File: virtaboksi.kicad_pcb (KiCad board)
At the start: 2 copper layers, 50 x 72 mm, 64 parts, among them J1 Panel_01x06, J2 External_01x06, J3 Optional_01x03, J5 Powerpole 01x02, J6 Powerpole 01x02, J7 Powerpole 01x02, J8 TagConnect_TC2030-NL, Q1 2N7002, Q2 IRF4905, Q3 IRF4905, Q4 2N7002, Q5 IRF4905, Q6 IRF4905, Q7 2N7002, Q8 IRF4905, Q9 IRF4905, U1 SRV05-4, U2 AMSRI-783.3-NZ, U3 SRV05-4, U4 SP3485EN, U5 STM8S003F3P

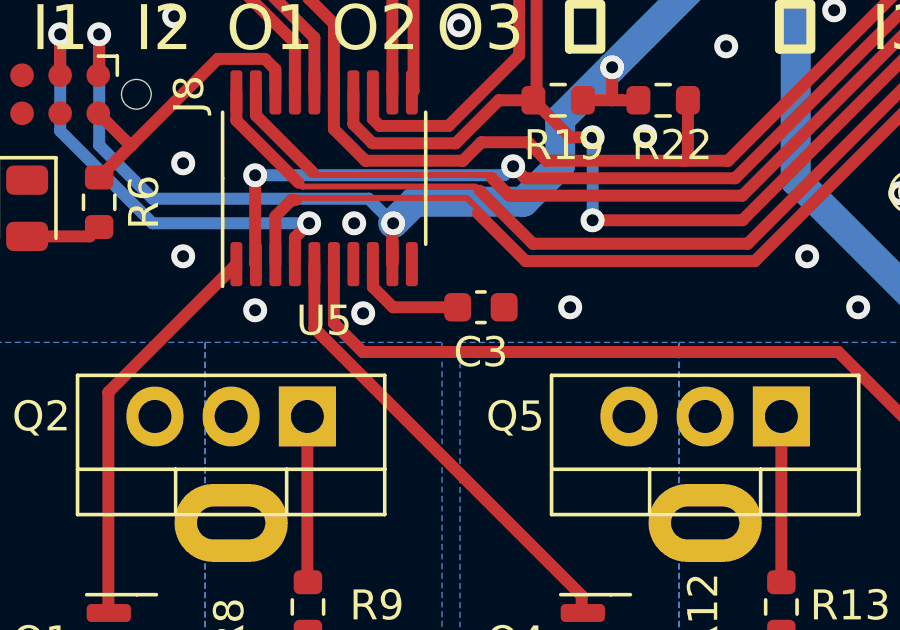
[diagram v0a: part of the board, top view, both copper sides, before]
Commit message: Move STM8S capacitor out of way
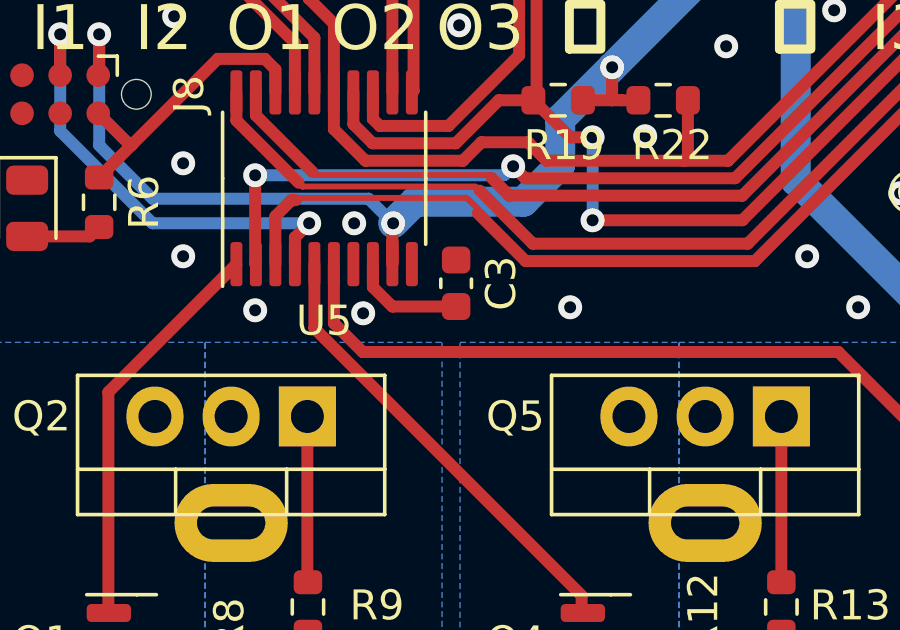
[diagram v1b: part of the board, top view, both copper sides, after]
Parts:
- moved C3 1.15 mm to (123.2, 61.9), turned to 90 degrees
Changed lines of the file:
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@@
   )
   (footprint "Capacitor_SMD:C_0603_1608Metric" (layer "F.Cu")
-    (at 124.025 62.7)
+    (at 123.2 61.9 90)
     (descr "Capacitor SMD 0603 (1608 Metric), square (rectangular) end terminal, IPC_7351 nominal, (Body size source: IPC-SM-782 page 76, https://www.pcb-3d.com/wordpress/wp-content/uploads/ipc-sm-782a_amendment_1_and_2.pdf), generated with kicad-footprint-generator")
     (tags "capacitor")
@@
     (property "Sheetname" "")
     (attr smd)
-    (fp_text reference "C3" (at 0 1.5) (layer "F.SilkS")
+    (fp_text reference "C3" (at 0 1.5 90) (layer "F.SilkS")
       (effects (font (size 1 1) (thickness 0.15)))
     )
-    (fp_text value "1u" (at 0 1.43) (layer "F.Fab")
+    (fp_text value "1u" (at 0 1.43 90) (layer "F.Fab")
       (effects (font (size 1 1) (thickness 0.15)))
     )
-    (fp_text user "${REFERENCE}" (at 0 0) (layer "F.Fab")
+    (fp_text user "${REFERENCE}" (at 0 0 90) (layer "F.Fab")
       (effects (font (size 0.4 0.4) (thickness 0.06)))
     )
@@
     (fp_line (start -0.8 0.4) (end -0.8 -0.4) (layer "F.Fab") (width 0.1))
     (fp_line (start -0.8 -0.4) (end 0.8 -0.4) (layer "F.Fab") (width 0.1))
-    (pad "1" smd roundrect (at -0.775 0) (size 0.9 0.95) (layers "F.Cu" "F.Paste" "F.Mask") (roundrect_rratio 0.25)
+    (pad "1" smd roundrect (at -0.775 0 90) (size 0.9 0.95) (layers "F.Cu" "F.Paste" "F.Mask") (roundrect_rratio 0.25)
       (net 8 "Net-(C3-Pad1)") (pintype "passive"))
-    (pad "2" smd roundrect (at 0.775 0) (size 0.9 0.95) (layers "F.Cu" "F.Paste" "F.Mask") (roundrect_rratio 0.25)
+    (pad "2" smd roundrect (at 0.775 0 90) (size 0.9 0.95) (layers "F.Cu" "F.Paste" "F.Mask") (roundrect_rratio 0.25)
       (net 1 "GND") (pintype "passive"))
     (model "${KICAD6_3DMODEL_DIR}/Capacitor_SMD.3dshapes/C_0603_1608Metric.wrl"
@@
   (segment (start 127.3825 72.85) (end 127.4225 72.89) (width 0.4) (layer "F.Cu") (net 7))
   (segment (start 118.475 61.2625) (end 118.475 63.400843) (width 0.4) (layer "F.Cu") (net 7))
-  (segment (start 121.096177 62.7) (end 123.25 62.7) (width 0.4) (layer "F.Cu") (net 8))
-  (segment (start 120.425 61.2625) (end 120.425 62.028823) (width 0.4) (layer "F.Cu") (net 8))
-  (segment (start 120.425 62.028823) (end 121.096177 62.7) (width 0.4) (layer "F.Cu") (net 8))
+  (segment (start 121.071177 62.675) (end 120.425 62.028823) (width 0.4) (layer "F.Cu") (net 8))
+  (segment (start 120.425 62.028823) (end 120.425 61.2625) (width 0.4) (layer "F.Cu") (net 8))
+  (segment (start 123.2 62.675) (end 121.071177 62.675) (width 0.4) (layer "F.Cu") (net 8))
   (segment (start 149.86 75.065) (end 151.71 76.915) (width 0.4) (layer "F.Cu") (net 9))
   (segment (start 147.14 76.615) (end 148.31 76.615) (width 0.4) (layer "F.Cu") (net 9))

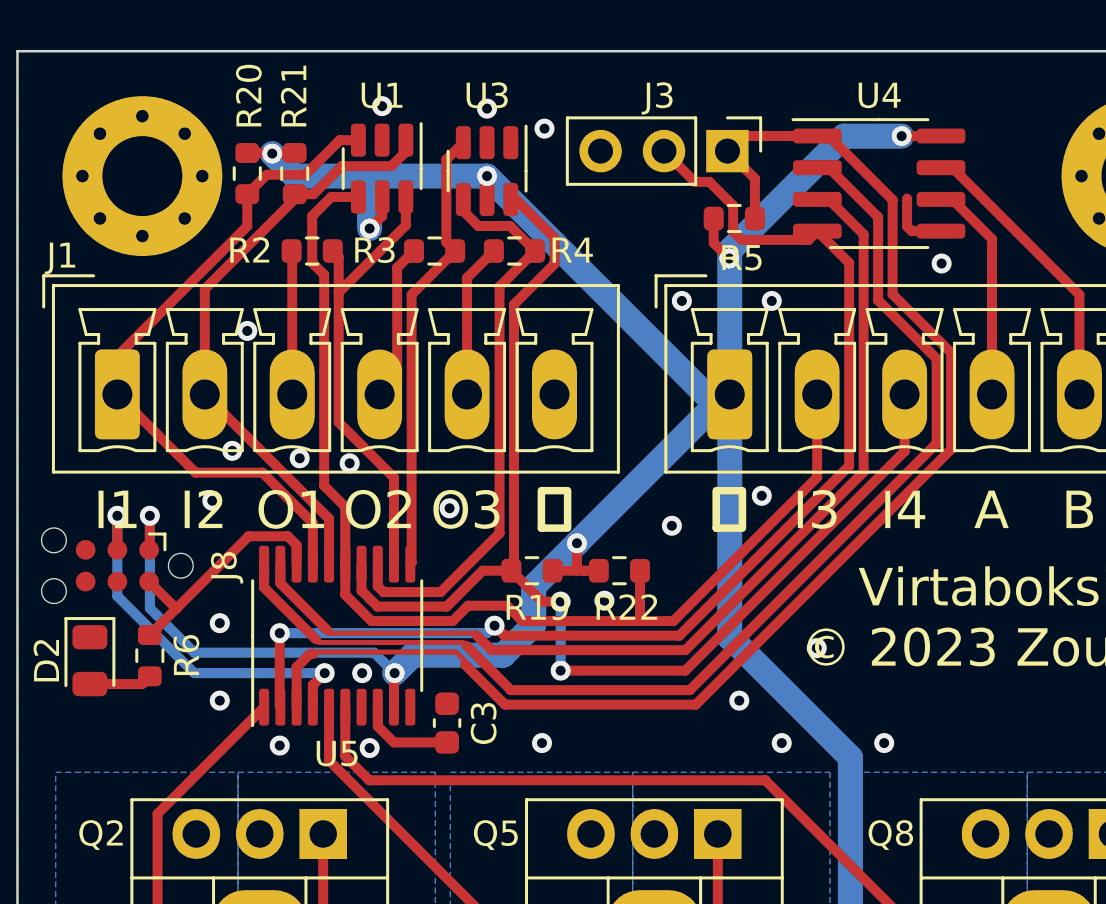
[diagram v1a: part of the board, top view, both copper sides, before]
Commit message: Final tweaks to the PCB. Swap LED pins for better routing.
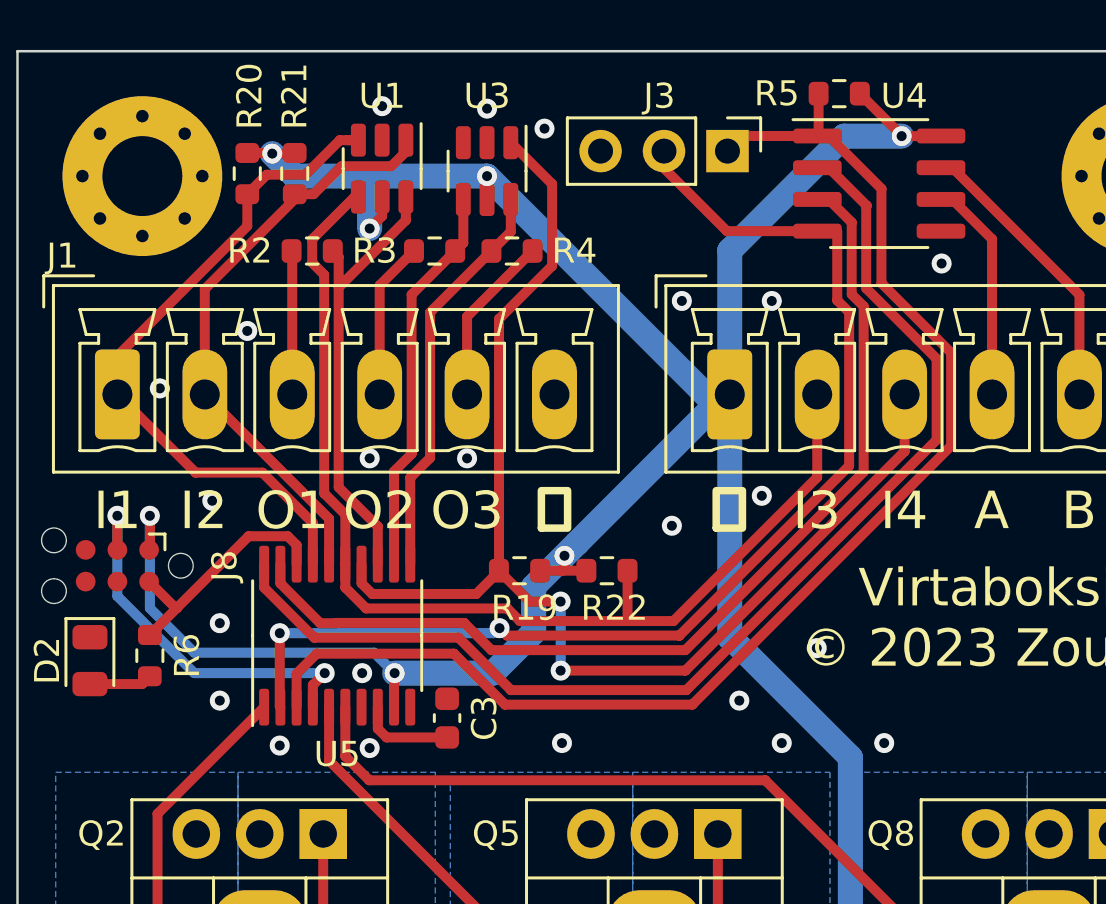
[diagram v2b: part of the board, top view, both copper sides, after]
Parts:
- moved R5 6.53 mm to (138.9, 36.7), turned to 180 degrees
- moved R19 0.50 mm to (126.1, 55.8)
- moved R22 0.50 mm to (129.6, 55.8)
- moved C3 0.20 mm to (123.2, 61.7)
- moved R4 0.10 mm to (125.8, 43.0), turned to 180 degrees
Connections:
- U3 pad 1: unconnected-(U3-Pad1) -> /IN4
- U3 pad 3: /LED2 -> unconnected-(U3-Pad3)
- U3 pad 4: /LED3 -> /LED2
- U3 pad 6: /IN4 -> /LED3
- U5 pad 11: /LED2 -> /LED3
- U5 pad 12: /LED1 -> /LED2
- U5 pad 13: /LED3 -> /LED1
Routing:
- net /LED3: track 22.7 -> 16.3 mm
- net GND: track 2.55 -> 0.00 mm, vias 29 -> 27
- net /LED2: track 18.0 -> 15.7 mm
- net /RX: track 56.0 -> 54.2 mm
- net /IN4: track 49.3 -> 51.0 mm
- net /IN3: track 45.5 -> 44.3 mm
- net Net-(J1-Pad5): track 6.19 -> 6.83 mm
- net +3.3V: track 153.7 -> 154.0 mm, vias 8 -> 7

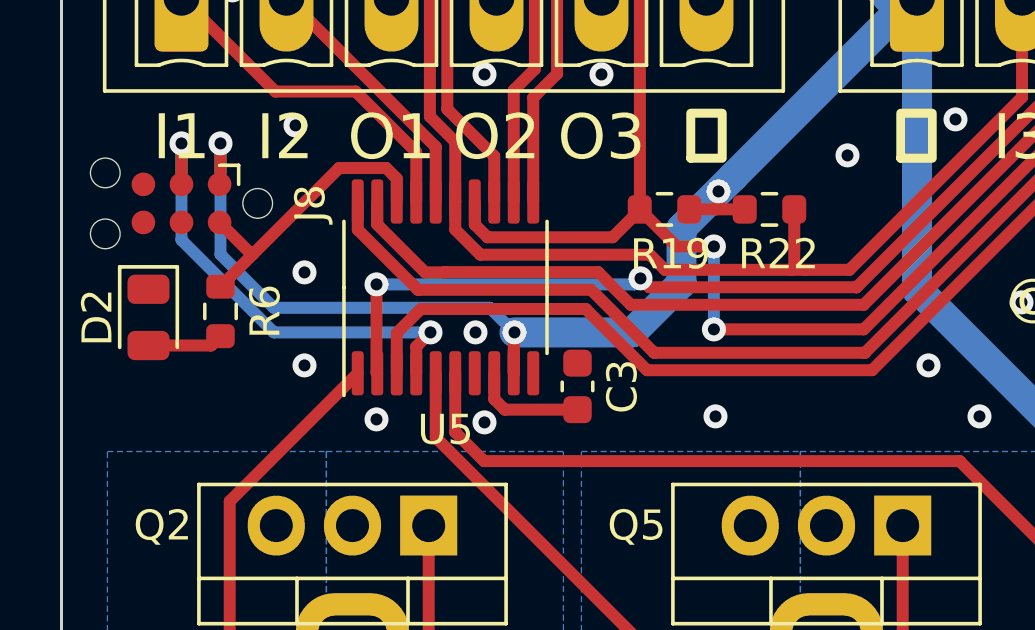
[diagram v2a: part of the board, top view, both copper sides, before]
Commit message: Move SMD LED so that it's not blocked by a heat sink
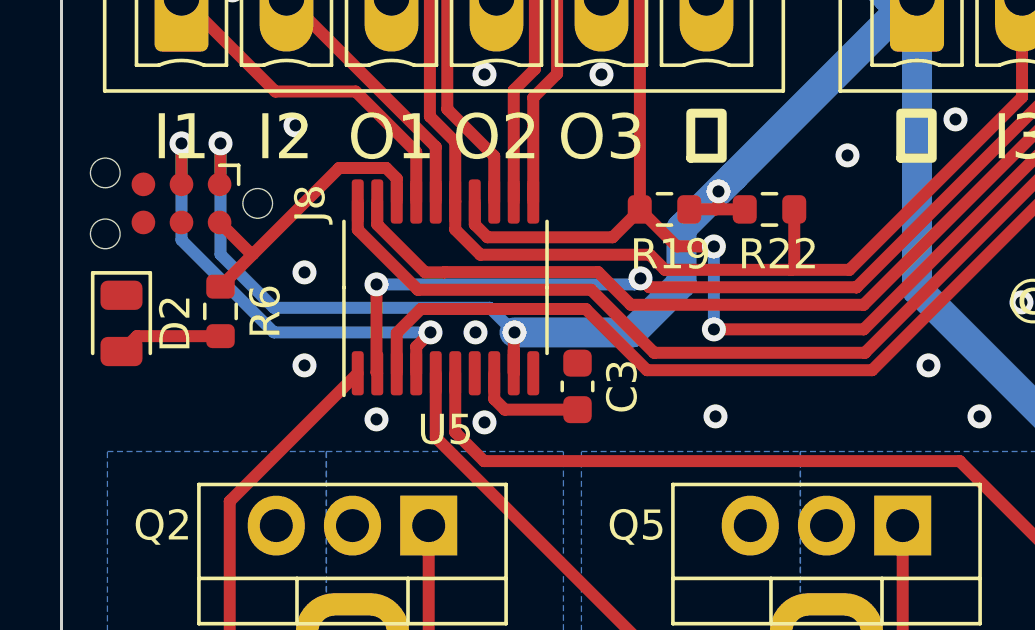
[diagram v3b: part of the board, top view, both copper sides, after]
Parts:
- moved D2 0.92 mm to (108.0, 59.6)
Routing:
- net Net-(D2-Pad2): track 2.53 -> 3.51 mm
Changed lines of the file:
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@@
   )
   (footprint "LED_SMD:LED_0805_2012Metric" (layer "F.Cu")
-    (at 108.9 59.4 -90)
+    (at 108 59.6 -90)
     (descr "LED SMD 0805 (2012 Metric), square (rectangular) end terminal, IPC_7351 nominal, (Body size source: https://docs.google.com/spreadsheets/d/1BsfQQcO9C6DZCsRaXUlFlo91Tg2WpOkGARC1WS5S8t0/edit?usp=sharing), generated with kicad-footprint-generator")
     (tags "LED")
@@
     (property "Sheetname" "")
     (attr smd)
-    (fp_text reference "D2" (at 0 1.7 90) (layer "F.SilkS")
+    (fp_text reference "D2" (at 0 -1.8 90) (layer "F.SilkS")
       (effects (font (size 1 1) (thickness 0.15)))
     )
@@
   (segment (start 138.0175 52.062256) (end 132.264756 57.815) (width 0.4) (layer "F.Cu") (net 11))
   (segment (start 118.28 52.702256) (end 119.125 53.547256) (width 0.4) (layer "F.Cu") (net 11))
-  (segment (start 130.785 57.815) (end 130.315 57.815) (width 0.4) (layer "F.Cu") (net 11))
+  (segment (start 130.315 57.815) (end 132.264756 57.815) (width 0.4) (layer "F.Cu") (net 11))
   (segment (start 117.8 43.470244) (end 118.28 43.950244) (width 0.4) (layer "F.Cu") (net 11))
   (segment (start 130.315 57.815) (end 126.118087 57.815) (width 0.4) (layer "F.Cu") (net 11))
@@
   (segment (start 119.960933 57.31) (end 119.125 56.474067) (width 0.4) (layer "F.Cu") (net 11))
   (segment (start 138.0175 48.7425) (end 138.0175 52.062256) (width 0.4) (layer "F.Cu") (net 11))
-  (segment (start 132.264756 57.815) (end 130.785 57.815) (width 0.4) (layer "F.Cu") (net 11))
   (segment (start 148.21 78.64) (end 146.51 78.64) (width 0.4) (layer "F.Cu") (net 12))
   (segment (start 145.0175 48.7425) (end 145.0175 42.522967) (width 0.4) (layer "F.Cu") (net 13))
@@
   (segment (start 111.6075 72.875) (end 111.6075 65.53) (width 0.4) (layer "F.Cu") (net 25))
   (segment (start 111.6075 65.53) (end 115.875 61.2625) (width 0.4) (layer "F.Cu") (net 25))
-  (segment (start 110.9875 60.3375) (end 111.3 60.025) (width 0.4) (layer "F.Cu") (net 26))
-  (segment (start 108.9 60.3375) (end 110.9875 60.3375) (width 0.4) (layer "F.Cu") (net 26))
+  (segment (start 111.3 60.025) (end 108.5125 60.025) (width 0.4) (layer "F.Cu") (net 26))
+  (segment (start 108.5125 60.025) (end 108 60.5375) (width 0.4) (layer "F.Cu") (net 26))
   (segment (start 115.64 75.065) (end 114.7225 75.065) (width 0.4) (layer "F.Cu") (net 27))
   (segment (start 114.7225 75.065) (end 113.4975 73.84) (width 0.4) (layer "F.Cu") (net 27))

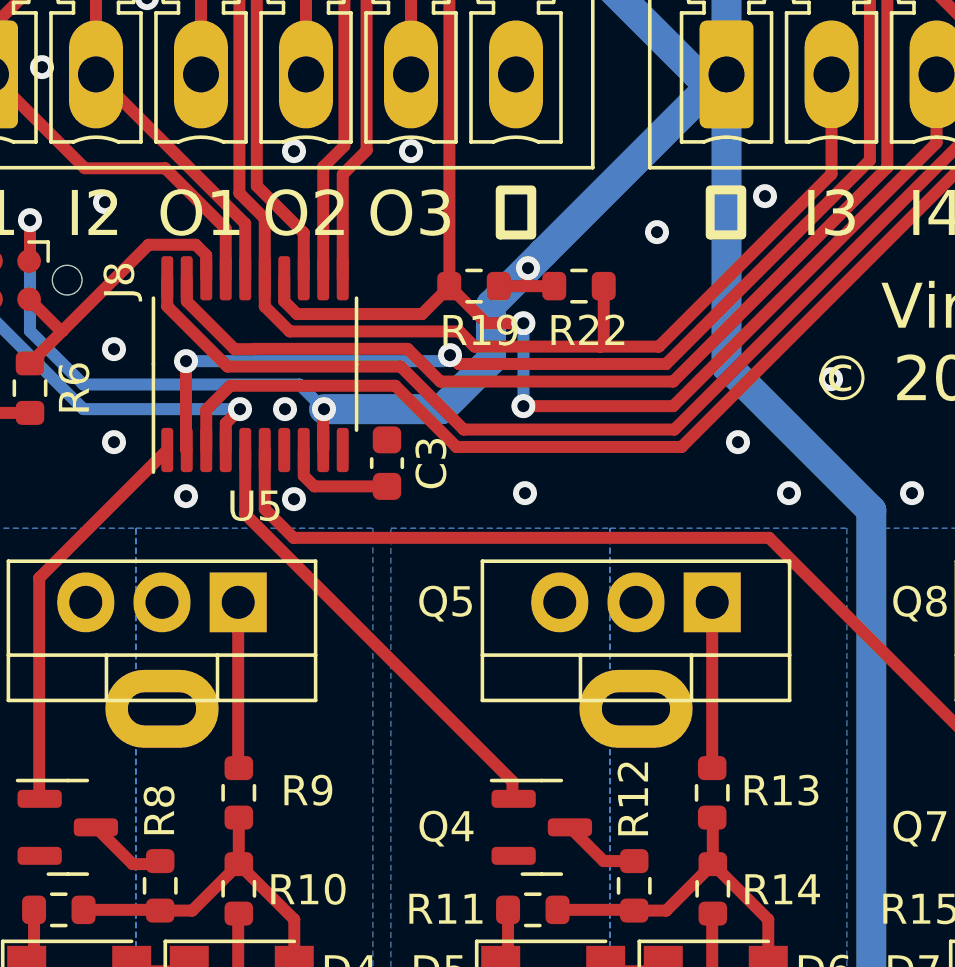
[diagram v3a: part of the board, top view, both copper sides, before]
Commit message: Evacuate output from PA1, not working with halt mode
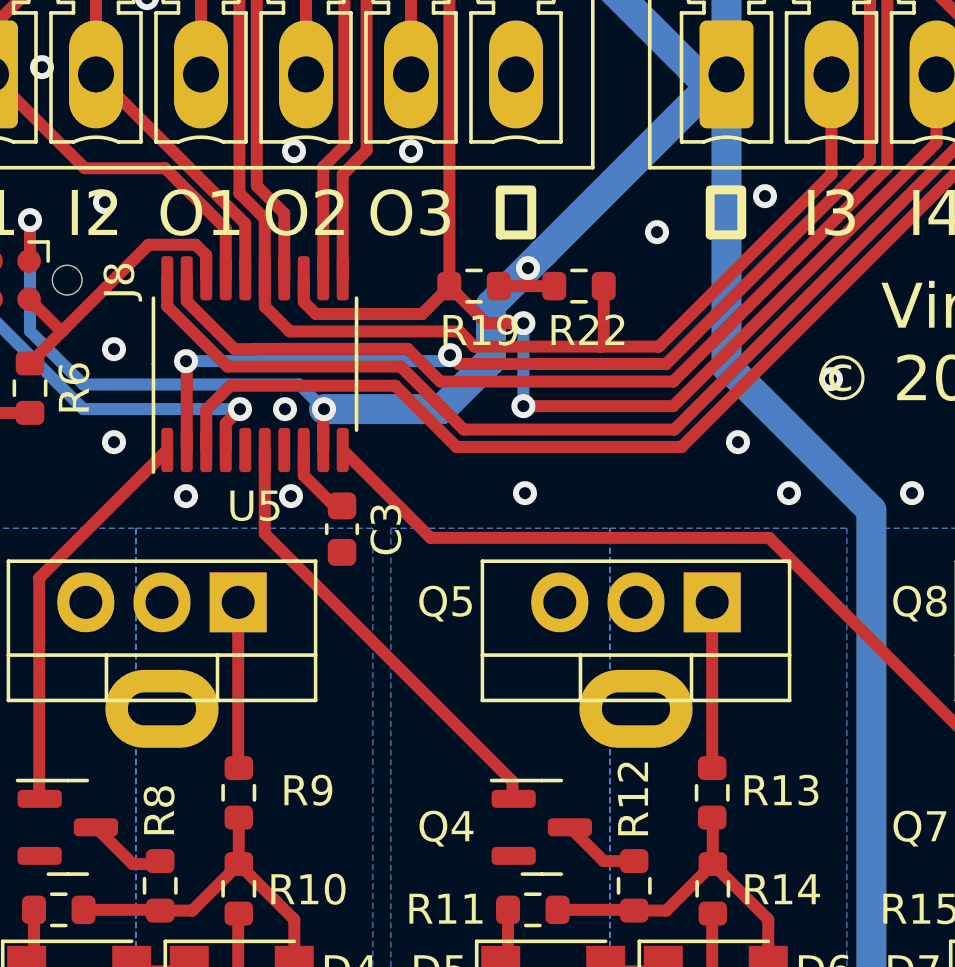
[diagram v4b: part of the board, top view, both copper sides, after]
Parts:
- moved C3 2.66 mm to (121.7, 63.9), turned to -90 degrees
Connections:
- U5 pad 10: unconnected-(U5-Pad10) -> /GROUP3 CTRL
- U5 pad 13: /LED1 -> /IN4
- U5 pad 14: /IN4 -> /LED1
- U5 pad 5: /GROUP2 CTRL -> unconnected-(U5-Pad5)
- U5 pad 6: /GROUP3 CTRL -> /GROUP2 CTRL
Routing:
- net /GROUP3 CTRL: track 30.9 -> 27.1 mm
- net Net-(C3-Pad1): track 3.78 -> 2.54 mm
- net /IN4: track 51.0 -> 50.3 mm
